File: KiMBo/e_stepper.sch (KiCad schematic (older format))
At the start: 24 parts, among them U21 TMC2130

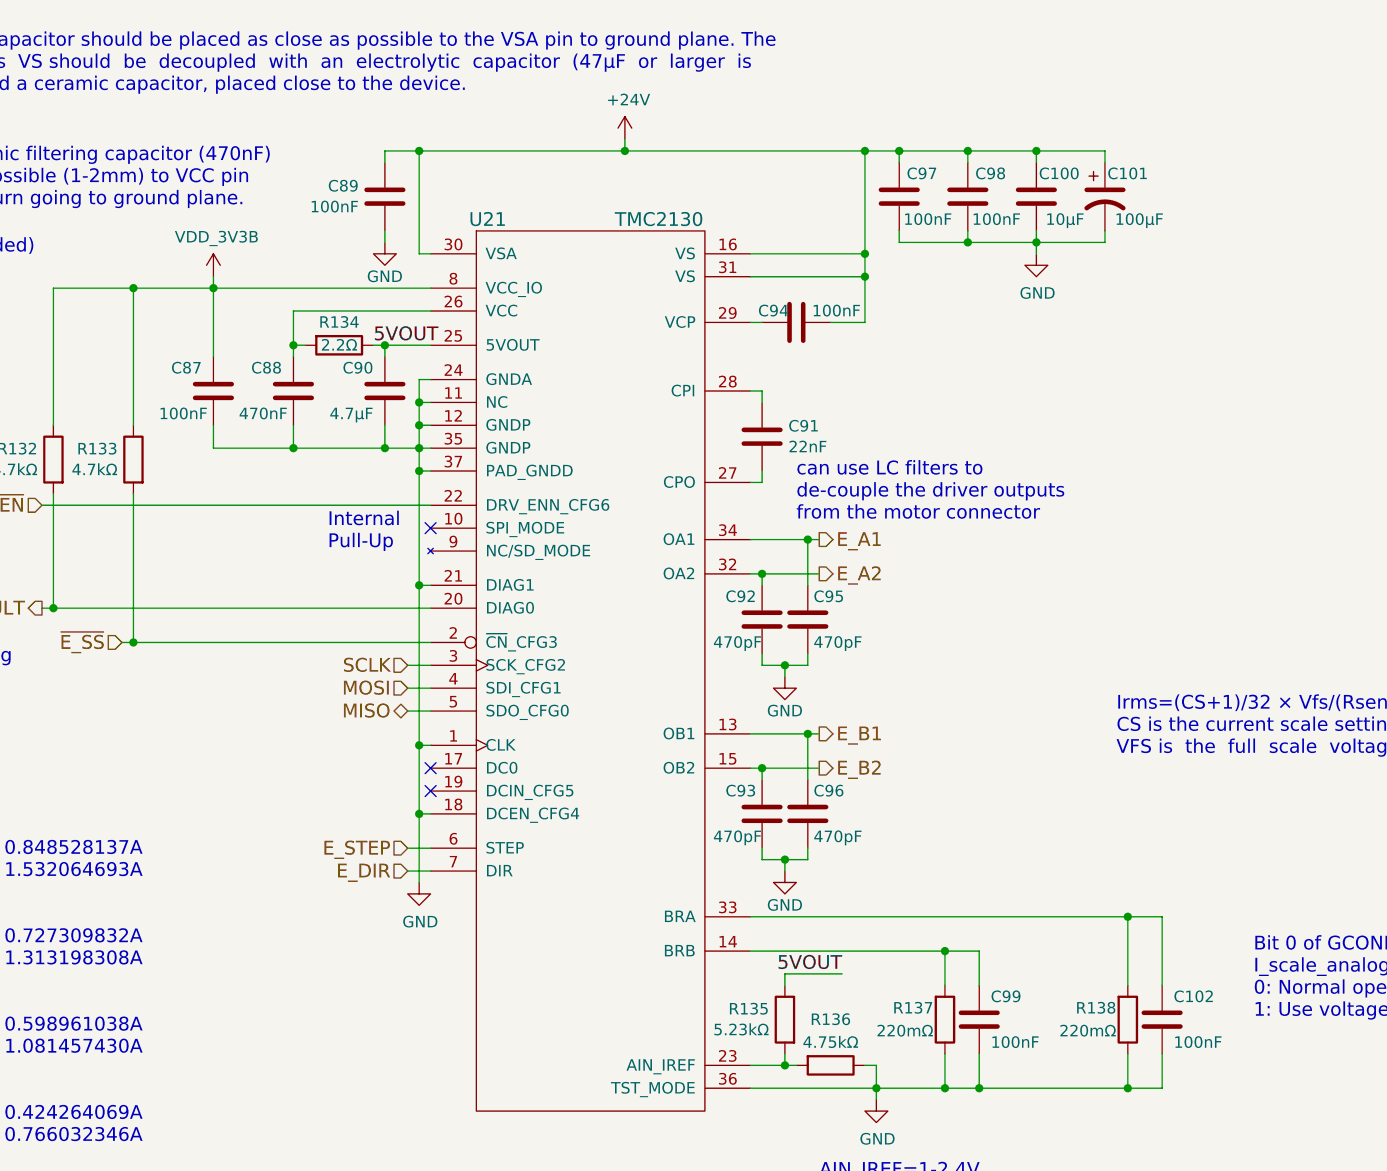
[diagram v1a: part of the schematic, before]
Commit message: Connect X and Z stepper driver open-drain DIAG0 and DIAG1 lines together
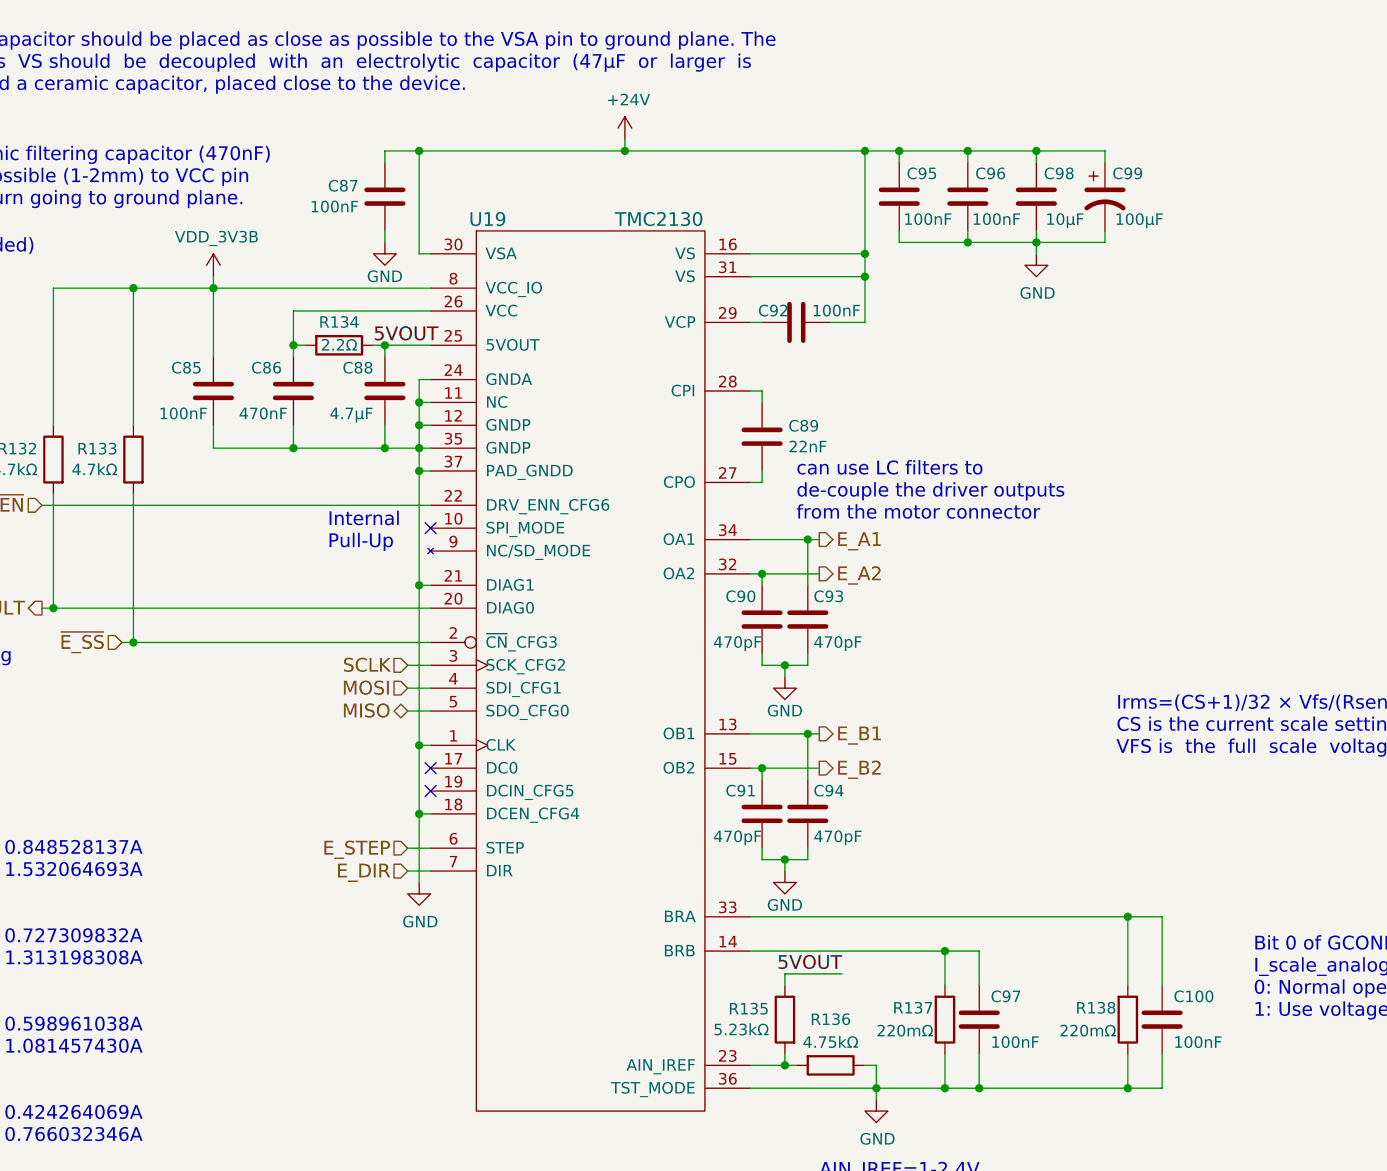
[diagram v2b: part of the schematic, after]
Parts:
- renumbered C102 to C100, C87 to C85, C88 to C86, C89 to C87, C90 to C88, C91 to C89, C92 to C90, C93 to C91, C94 to C92, C95 to C93, C96 to C94, C97 to C95, C98 to C96, C99 to C97, C100 to C98, C101 to C99, U21 to U19
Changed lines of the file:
@@
 MOSI
 $Comp
-L C C89
+L C C87
 U 1 1 589B8A74
 P 7300 3950
-F 0 "C89" H 7186 3904 50  0000 R CNN
+F 0 "C87" H 7186 3904 50  0000 R CNN
 F 1 "100nF" H 7186 3995 50  0000 R CNN
 F 2 "Capacitors_SMD:C_0603" H 7338 3800 50  0001 C CNN
@@
 $EndComp
 $Comp
-L C C94
+L C C92
 U 1 1 5BA7E11F
 P 9100 4500
-F 0 "C94" V 9050 4400 50  0000 C CNN
+F 0 "C92" V 9050 4400 50  0000 C CNN
 F 1 "100nF" V 9050 4675 50  0000 C CNN
 F 2 "Capacitors_SMD:C_0603" H 9138 4350 50  0001 C CNN
@@
 $EndComp
 $Comp
-L CP1 C101
+L CP1 C99
 U 1 1 5BA7E120
 P 10450 3950
-F 0 "C101" H 10550 4050 50  0000 C CNN
+F 0 "C99" H 10550 4050 50  0000 C CNN
 F 1 "100μF" H 10600 3850 50  0000 C CNN
 F 2 "Capacitors_SMD:c_elec_8x10" H 10450 3950 50  0001 C CNN
@@
 $EndComp
 $Comp
-L C C97
+L C C95
 U 1 1 589BC941
 P 9550 3950
-F 0 "C97" H 9450 4050 50  0000 C CNN
+F 0 "C95" H 9450 4050 50  0000 C CNN
 F 1 "100nF" H 9425 3850 50  0000 C CNN
 F 2 "Capacitors_SMD:C_0603" H 9588 3800 50  0001 C CNN
@@
 $EndComp
 $Comp
-L GND #PWR0210
+L GND #PWR0200
 U 1 1 589BD203
 P 7300 4150
-F 0 "#PWR0210" H 7300 3900 50  0001 C CNN
+F 0 "#PWR0200" H 7300 3900 50  0001 C CNN
 F 1 "GND" H 7300 4000 50  0000 C CNN
 F 2 "" H 7300 4150 50  0000 C CNN
@@
 $EndComp
 $Comp
-L C C98
+L C C96
 U 1 1 589BDAA2
 P 9850 3950
-F 0 "C98" H 9750 4050 50  0000 C CNN
+F 0 "C96" H 9750 4050 50  0000 C CNN
 F 1 "100nF" H 9725 3850 50  0000 C CNN
 F 2 "Capacitors_SMD:C_0603" H 9888 3800 50  0001 C CNN
@@
 $EndComp
 $Comp
-L GND #PWR0211
+L GND #PWR0201
 U 1 1 589BE47E
 P 10150 4200
-F 0 "#PWR0211" H 10150 3950 50  0001 C CNN
+F 0 "#PWR0201" H 10150 3950 50  0001 C CNN
 F 1 "GND" H 10155 4027 50  0000 C CNN
 F 2 "" H 10150 4200 50  0000 C CNN
@@
 $EndComp
 $Comp
-L +24V #PWR0212
+L +24V #PWR0202
 U 1 1 5BA7E125
 P 8350 3700
-F 0 "#PWR0212" H 8350 3550 50  0001 C CNN
+F 0 "#PWR0202" H 8350 3550 50  0001 C CNN
 F 1 "+24V" H 8365 3873 50  0000 C CNN
 F 2 "" H 8350 3700 50  0000 C CNN
@@
 $EndComp
 $Comp
-L C C91
+L C C89
 U 1 1 589C0BAD
 P 8950 5000
-F 0 "C91" H 9065 5046 50  0000 L CNN
+F 0 "C89" H 9065 5046 50  0000 L CNN
 F 1 "22nF" H 9065 4955 50  0000 L CNN
 F 2 "Capacitors_SMD:C_0402" H 8988 4850 50  0001 C CNN
@@
 $EndComp
 $Comp
-L GND #PWR0213
+L GND #PWR0203
 U 1 1 5BA7E129
 P 9450 7900
-F 0 "#PWR0213" H 9450 7650 50  0001 C CNN
+F 0 "#PWR0203" H 9450 7650 50  0001 C CNN
 F 1 "GND" H 9455 7727 50  0000 C CNN
 F 2 "" H 9450 7900 50  0000 C CNN
@@
 $EndComp
 $Comp
-L C C88
+L C C86
 U 1 1 589C52DF
 P 6900 4800
-F 0 "C88" H 6950 4900 50  0000 L CNN
+F 0 "C86" H 6950 4900 50  0000 L CNN
 F 1 "470nF" H 6925 4700 50  0000 L CNN
 F 2 "Capacitors_SMD:C_0603" H 6938 4650 50  0001 C CNN
@@
 NoConn ~ 7500 6550
 $Comp
-L GND #PWR0214
+L GND #PWR0204
 U 1 1 589C97FF
 P 7450 6950
-F 0 "#PWR0214" H 7450 6700 50  0001 C CNN
+F 0 "#PWR0204" H 7450 6700 50  0001 C CNN
 F 1 "GND" H 7455 6777 50  0000 C CNN
 F 2 "" H 7450 6950 50  0000 C CNN
@@
 $EndComp
 $Comp
-L C C99
+L C C97
 U 1 1 5BA7E12E
 P 9900 7550
-F 0 "C99" H 9950 7650 50  0000 L CNN
+F 0 "C97" H 9950 7650 50  0000 L CNN
 F 1 "100nF" H 9950 7450 50  0000 L CNN
 F 2 "Capacitors_SMD:C_0603" H 9938 7400 50  0001 C CNN
@@
 Internal\nPull-Up
 $Comp
-L C C90
+L C C88
 U 1 1 5BA7E12A
 P 7300 4800
-F 0 "C90" H 7350 4900 50  0000 L CNN
+F 0 "C88" H 7350 4900 50  0000 L CNN
 F 1 "4.7μF" H 7350 4700 50  0000 L CNN
 F 2 "Capacitors_SMD:C_0402" H 7338 4650 50  0001 C CNN
@@
 $EndComp
 $Comp
-L C C102
+L C C100
 U 1 1 5BA7E133
 P 10700 7550
-F 0 "C102" H 10750 7650 50  0000 L CNN
+F 0 "C100" H 10750 7650 50  0000 L CNN
 F 1 "100nF" H 10750 7450 50  0000 L CNN
 F 2 "Capacitors_SMD:C_0603" H 10738 7400 50  0001 C CNN
@@
 Choose  sense  resistors  in  a  way,  that  normal \nIRUN is 16 to 31 for best microstep performance.
 $Comp
-L C C92
+L C C90
 U 1 1 5BA7E134
 P 8950 5800
-F 0 "C92" H 8975 5900 50  0000 L CNN
+F 0 "C90" H 8975 5900 50  0000 L CNN
 F 1 "470pF" H 8950 5700 50  0000 L CNN
 F 2 "Capacitors_SMD:C_0603" H 8988 5650 50  0001 C CNN
@@
 $EndComp
 $Comp
-L GND #PWR0215
+L GND #PWR0205
 U 1 1 58B19D33
 P 9050 6050
-F 0 "#PWR0215" H 9050 5800 50  0001 C CNN
+F 0 "#PWR0205" H 9050 5800 50  0001 C CNN
 F 1 "GND" H 9050 5900 50  0000 C CNN
 F 2 "" H 9050 6050 50  0000 C CNN
@@
 $EndComp
 $Comp
-L C C95
+L C C93
 U 1 1 58B1B794
 P 9150 5800
-F 0 "C95" H 9175 5900 50  0000 L CNN
+F 0 "C93" H 9175 5900 50  0000 L CNN
 F 1 "470pF" H 9175 5700 50  0000 L CNN
 F 2 "Capacitors_SMD:C_0603" H 9188 5650 50  0001 C CNN
@@
 $EndComp
 $Comp
-L C C93
+L C C91
 U 1 1 58B1C6FD
 P 8950 6650
-F 0 "C93" H 8975 6750 50  0000 L CNN
+F 0 "C91" H 8975 6750 50  0000 L CNN
 F 1 "470pF" H 8950 6550 50  0000 L CNN
 F 2 "Capacitors_SMD:C_0603" H 8988 6500 50  0001 C CNN
@@
 $EndComp
 $Comp
-L GND #PWR0216
+L GND #PWR0206
 U 1 1 58B1C704
 P 9050 6900
-F 0 "#PWR0216" H 9050 6650 50  0001 C CNN
+F 0 "#PWR0206" H 9050 6650 50  0001 C CNN
 F 1 "GND" H 9050 6750 50  0000 C CNN
 F 2 "" H 9050 6900 50  0000 C CNN
@@
 $EndComp
 $Comp
-L C C96
+L C C94
 U 1 1 58B1C710
 P 9150 6650
-F 0 "C96" H 9175 6750 50  0000 L CNN
+F 0 "C94" H 9175 6750 50  0000 L CNN
 F 1 "470pF" H 9175 6550 50  0000 L CNN
 F 2 "Capacitors_SMD:C_0603" H 9188 6500 50  0001 C CNN
@@
 $EndComp
 $Comp
-L TMC2130 U21
+L TMC2130 U19
 U 1 1 5BA7E11D
 P 8200 5550
-F 0 "U21" H 7750 7050 60  0000 C CNN
+F 0 "U19" H 7750 7050 60  0000 C CNN
 F 1 "TMC2130" H 8500 7050 60  0000 C CNN
 F 2 "" H 8200 5850 60  0001 C CNN
@@
 $EndComp
 $Comp
-L C C100
+L C C98
 U 1 1 58B40194
 P 10150 3950
-F 0 "C100" H 10050 4050 50  0000 C CNN
+F 0 "C98" H 10050 4050 50  0000 C CNN
 F 1 "10μF" H 10025 3850 50  0000 C CNN
 F 2 "Capacitors_SMD:C_0805" H 10188 3800 50  0001 C CNN
@@
 Can extract which\nfault is occurring via SPI\nby reading DRV_STATUS reg
 $Comp
-L VDD_3V3B #PWR0217
+L VDD_3V3B #PWR0207
 U 1 1 5A2FD350
 P 6550 4300
-F 0 "#PWR0217" H 6550 4150 50  0001 C CNN
+F 0 "#PWR0207" H 6550 4150 50  0001 C CNN
 F 1 "VDD_3V3B" H 6565 4473 50  0000 C CNN
 F 2 "" H 6550 4300 50  0000 C CNN
@@
 $EndComp
 $Comp
-L C C87
+L C C85
 U 1 1 5A896678
 P 6550 4800
-F 0 "C87" H 6600 4900 50  0000 L CNN
+F 0 "C85" H 6600 4900 50  0000 L CNN
 F 1 "100nF" H 6575 4700 50  0000 L CNN
 F 2 "Capacitors_SMD:C_0603" H 6588 4650 50  0001 C CNN
